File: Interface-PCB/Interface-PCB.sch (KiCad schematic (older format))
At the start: 14 parts, among them J1 BARREL_JACK_PAD, J2 BARREL_JACK_PAD, J3 GPIO_DEBUG_HEADER, J4 RASPBERRYPI_GPIO_CONN_HEADER, J5 I2C_HEADER, M1 PERISTALTIC_PUMP, M2 PERISTALTIC_PUMP, M3 PERISTALTIC_PUMP, U1 TB6612FNG_BREAKOUT, U2 TB6612FNG_BREAKOUT

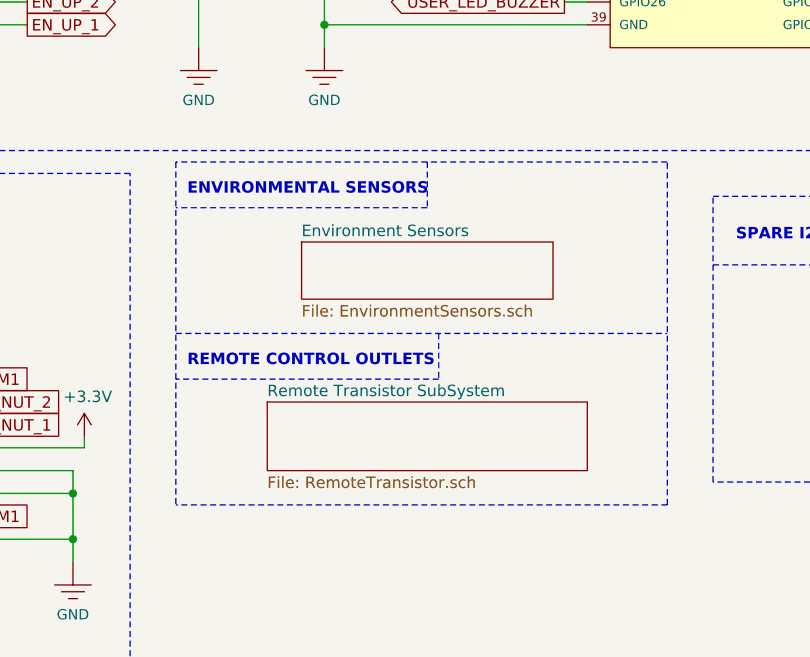
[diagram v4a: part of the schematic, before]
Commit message: Add indicator LEDs
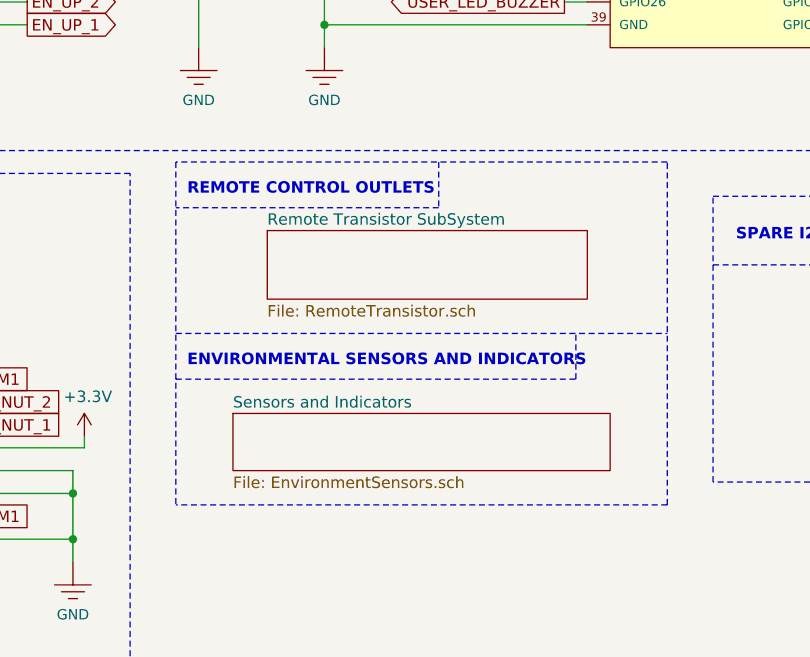
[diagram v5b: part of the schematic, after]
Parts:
- U1: footprint digikey-footprints:DIP-16_W7.62mm -> Package_DIP:DIP-16_W7.62mm_LongPads
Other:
- note added: "ENVIRONMENTAL SENSORS AND INDICATORS"
- note removed: "ENVIRONMENTAL SENSORS"
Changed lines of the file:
@@
 F 0 "U1" H 2300 7167 50  0000 C CNN
 F 1 "TB6612FNG_BREAKOUT" H 2300 7076 50  0000 C CNN
-F 2 "digikey-footprints:DIP-16_W7.62mm" H 1750 6800 50  0001 L CNN
+F 2 "Package_DIP:DIP-16_W7.62mm_LongPads" H 1750 6800 50  0001 L CNN
 F 3 "" H 2450 6800 50  0001 C CNN
 	1    2300 6550
@@
 $EndComp
 $Comp
-L power:+3.3V #PWR02
+L power:+3.3V #PWR03
 U 1 1 63904DA3
 P 1700 6150
-F 0 "#PWR02" H 1700 6000 50  0001 C CNN
+F 0 "#PWR03" H 1700 6000 50  0001 C CNN
 F 1 "+3.3V" H 1715 6323 50  0000 C CNN
 F 2 "" H 1700 6150 50  0001 C CNN
@@
 pH Up
 $Comp
-L power:+3.3V #PWR05
+L power:+3.3V #PWR06
 U 1 1 639CCEC1
 P 3400 6400
-F 0 "#PWR05" H 3400 6250 50  0001 C CNN
+F 0 "#PWR06" H 3400 6250 50  0001 C CNN
 F 1 "+3.3V" H 3415 6573 50  0000 C CNN
 F 2 "" H 3400 6400 50  0001 C CNN
@@
 $EndComp
 $Comp
-L power:+3.3V #PWR07
+L power:+3.3V #PWR08
 U 1 1 63A48F33
 P 4300 6150
-F 0 "#PWR07" H 4300 6000 50  0001 C CNN
+F 0 "#PWR08" H 4300 6000 50  0001 C CNN
 F 1 "+3.3V" H 4315 6323 50  0000 C CNN
 F 2 "" H 4300 6150 50  0001 C CNN
@@
 Note: Motors connect via Deans Connectors
 $Comp
-L power:+12V #PWR03
+L power:+12V #PWR02
 U 1 1 63B7D3C4
 P 1700 3600
-F 0 "#PWR03" H 1700 3450 50  0001 C CNN
+F 0 "#PWR02" H 1700 3450 50  0001 C CNN
 F 1 "+12V" H 1715 3773 50  0000 C CNN
 F 2 "" H 1700 3600 50  0001 C CNN
@@
 Wire Wire Line
 	9800 5950 9650 5950
-Text Notes 6450 5350 0    50   ~ 10
-ENVIRONMENTAL SENSORS
+Text Notes 6450 6100 0    50   ~ 10
+ENVIRONMENTAL SENSORS AND INDICATORS
 $Sheet
-S 6800 6250 1400 300
+S 6800 5500 1400 300
 U 6373D3AE
 F0 "Remote Transistor SubSystem" 50
@@
 Wire Notes Line
 	8550 5200 6400 5200
-$Sheet
-S 6950 5550 1100 250
-U 6375997B
-F0 "Environment Sensors" 50
-F1 "EnvironmentSensors.sch" 50
-$EndSheet
-Text Notes 6450 6100 0    50   ~ 10
+Text Notes 6450 5350 0    50   ~ 10
 REMOTE CONTROL OUTLETS
 NoConn ~ 4450 6750
@@
 LEVEL_PH_DOWN_3V3
 $Comp
-L power:+3.3V #PWR08
+L power:+3.3V #PWR07
 U 1 1 63CEAD9F
 P 4300 2550
-F 0 "#PWR08" H 4300 2400 50  0001 C CNN
+F 0 "#PWR07" H 4300 2400 50  0001 C CNN
 F 1 "+3.3V" H 4315 2723 50  0000 C CNN
 F 2 "" H 4300 2550 50  0001 C CNN
@@
 	6500 3300 6500 3600
 $Comp
-L power:+3.3V #PWR06
+L power:+3.3V #PWR05
 U 1 1 63CEAE0E
 P 3400 3350
-F 0 "#PWR06" H 3400 3200 50  0001 C CNN
+F 0 "#PWR05" H 3400 3200 50  0001 C CNN
 F 1 "+3.3V" H 3415 3523 50  0000 C CNN
 F 2 "" H 3400 3350 50  0001 C CNN
@@
 	6400 5200 6400 6700
 Wire Notes Line
-	7500 5200 7500 5400
-Wire Notes Line
-	7500 5400 6400 5400
-Wire Notes Line
-	7550 5950 7550 6150
-Wire Notes Line
-	7550 6150 6400 6150
+	7550 5200 7550 5400
+Wire Notes Line
+	7550 5400 6400 5400
 Wire Notes Line
 	8750 5350 10350 5350
@@
 Wire Notes Line
 	1550 4650 1550 4450
+Wire Notes Line
+	6400 6150 8150 6150
+Wire Notes Line
+	8150 6150 8150 5950
+$Sheet
+S 6650 6300 1650 250
+U 6375997B
+F0 "Sensors and Indicators" 50
+F1 "EnvironmentSensors.sch" 50
+$EndSheet
 $EndSCHEMATC
